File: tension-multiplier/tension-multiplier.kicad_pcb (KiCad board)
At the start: 2 copper layers, 18 x 13 mm, 4 parts, among them J1 Conn_01x03_Pin, J2 Conn_01x02_Pin, J3 Conn_01x02_Pin, U1 AD633ARZ

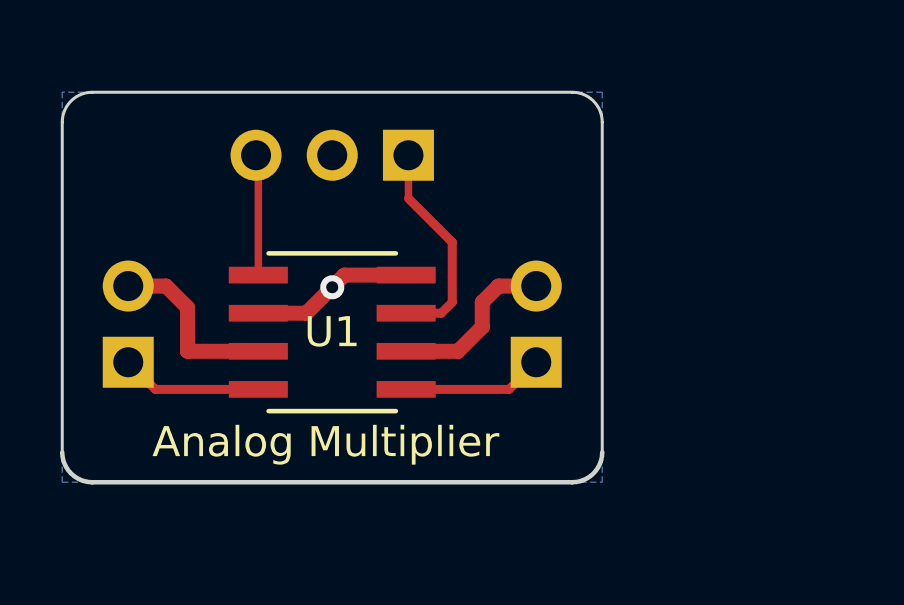
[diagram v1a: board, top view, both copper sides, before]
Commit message: Changes dimentions of the tension multiplier
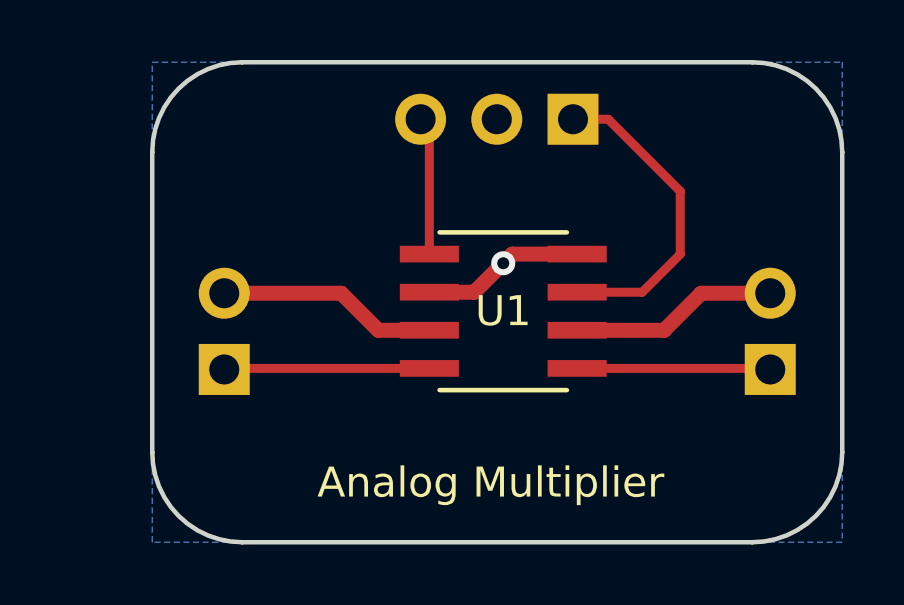
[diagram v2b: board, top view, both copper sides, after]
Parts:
- moved J2 7.80 mm to (158.6, 90.2)
- moved U1 5.74 mm to (149.7, 88.3)
- moved J1 5.61 mm to (152.0, 81.9)
- moved J3 3.21 mm to (140.4, 90.2)
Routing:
- net Net-(J1-Pin_1): track 7.19 -> 10.6 mm
- net Net-(J3-Pin_1): track 4.71 -> 6.85 mm
- net Net-(J2-Pin_1): track 4.71 -> 6.45 mm
- net VEE: track 6.09 -> 7.35 mm
- net VDD: track 5.72 -> 6.95 mm
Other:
- board size 18 x 13 mm -> 23 x 16 mm
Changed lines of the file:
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@@
   (net 7 "VEE")
   (footprint "footprints:R_8_ADI" (layer "F.Cu")
-    (at 144 89)
+    (at 149.7 88.3)
     (tags "AD633ARZ ")
     (property "Sheetfile" "tension-multiplier.kicad_sch")
@@
   )
   (footprint "Connector_PinHeader_2.54mm:PinHeader_1x03_P2.54mm_Vertical" (layer "B.Cu")
-    (at 146.54 83.1 90)
+    (at 152.025 81.9 90)
     (descr "Through hole straight pin header, 1x03, 2.54mm pitch, single row")
     (tags "Through hole pin header THT 1x03 2.54mm single row")
@@
   )
   (footprint "Connector_PinHeader_2.54mm:PinHeader_1x02_P2.54mm_Vertical" (layer "B.Cu")
-    (at 137.2 90)
+    (at 140.4 90.24)
     (descr "Through hole straight pin header, 1x02, 2.54mm pitch, single row")
     (tags "Through hole pin header THT 1x02 2.54mm single row")
@@
   )
   (footprint "Connector_PinHeader_2.54mm:PinHeader_1x02_P2.54mm_Vertical" (layer "B.Cu")
-    (at 150.8 90)
+    (at 158.6 90.24)
     (descr "Through hole straight pin header, 1x02, 2.54mm pitch, single row")
     (tags "Through hole pin header THT 1x02 2.54mm single row")
@@
     )
   )
-  (gr_line (start 135 93) (end 135 82)
-    (stroke (width 0.1) (type default)) (layer "Edge.Cuts"))
-  (gr_line (start 136 94) (end 152 94)
-    (stroke (width 0.15) (type default)) (layer "Edge.Cuts"))
-  (gr_line (start 136 81) (end 152 81)
-    (stroke (width 0.1) (type default)) (layer "Edge.Cuts"))
-  (gr_arc (start 135 82) (mid 135.292893 81.292893) (end 136 81)
-    (stroke (width 0.1) (type default)) (layer "Edge.Cuts"))
-  (gr_arc (start 152 81) (mid 152.707107 81.292893) (end 153 82)
-    (stroke (width 0.1) (type default)) (layer "Edge.Cuts"))
-  (gr_arc (start 136 94) (mid 135.292894 93.707107) (end 135 93)
-    (stroke (width 0.15) (type default)) (layer "Edge.Cuts"))
-  (gr_arc (start 153 93) (mid 152.707107 93.707106) (end 152 94)
-    (stroke (width 0.15) (type default)) (layer "Edge.Cuts"))
-  (gr_line (start 153 93) (end 153 82)
-    (stroke (width 0.1) (type default)) (layer "Edge.Cuts"))
-  (gr_text "Ux" (at 148 86) (layer "B.SilkS")
+  (gr_arc (start 161 93) (mid 160.12132 95.12132) (end 158 96)
+    (stroke (width 0.15) (type default)) (layer "Edge.Cuts"))
+  (gr_line (start 161 93) (end 161 83)
+    (stroke (width 0.15) (type default)) (layer "Edge.Cuts"))
+  (gr_line (start 141 96) (end 158 96)
+    (stroke (width 0.15) (type default)) (layer "Edge.Cuts"))
+  (gr_line (start 141 80) (end 158 80)
+    (stroke (width 0.15) (type default)) (layer "Edge.Cuts"))
+  (gr_arc (start 138 83) (mid 138.87868 80.87868) (end 141 80)
+    (stroke (width 0.15) (type default)) (layer "Edge.Cuts"))
+  (gr_arc (start 158 80) (mid 160.12132 80.87868) (end 161 83)
+    (stroke (width 0.15) (type default)) (layer "Edge.Cuts"))
+  (gr_arc (start 141 96) (mid 138.87868 95.12132) (end 138 93)
+    (stroke (width 0.15) (type default)) (layer "Edge.Cuts"))
+  (gr_line (start 138 93) (end 138 83)
+    (stroke (width 0.15) (type default)) (layer "Edge.Cuts"))
+  (gr_text "Ux" (at 153.66 84.8) (layer "B.SilkS")
     (effects (font (size 1 1) (thickness 0.2)) (justify left bottom mirror))
   )
-  (gr_text "Uz" (at 141 90.5) (layer "B.SilkS")
+  (gr_text "Uz" (at 144.1 90.74) (layer "B.SilkS")
     (effects (font (size 1 1) (thickness 0.2) bold) (justify left bottom mirror))
   )
-  (gr_text "V-" (at 141 88) (layer "B.SilkS")
+  (gr_text "V-" (at 144.2 88.24) (layer "B.SilkS")
     (effects (font (size 1 1) (thickness 0.2)) (justify left bottom mirror))
   )
-  (gr_text "Uw" (at 149 90.5) (layer "B.SilkS")
+  (gr_text "Uw" (at 156.6 90.7) (layer "B.SilkS")
     (effects (font (size 1 1) (thickness 0.2) bold) (justify left bottom mirror))
   )
-  (gr_text "V+" (at 149 88) (layer "B.SilkS")
+  (gr_text "V+" (at 156.8 88.24) (layer "B.SilkS")
     (effects (font (size 1 1) (thickness 0.2) bold) (justify left bottom mirror))
   )
-  (gr_text "Uy" (at 141.5 86) (layer "B.SilkS")
+  (gr_text "Uy" (at 147.16 84.8) (layer "B.SilkS")
     (effects (font (size 1 1) (thickness 0.2) bold) (justify left bottom mirror))
   )
-  (gr_text "GND" (at 145.5 86) (layer "B.SilkS")
+  (gr_text "GND" (at 151.16 84.8) (layer "B.SilkS")
     (effects (font (size 1 1) (thickness 0.2) bold) (justify left bottom mirror))
   )
-  (gr_text "Analog Multiplier" (at 138 93.25) (layer "F.SilkS")
+  (gr_text "Analog Multiplier" (at 143.5 94.6) (layer "F.SilkS")
     (effects (font (size 1 1) (thickness 0.2)) (justify left bottom))
   )
-  (segment (start 148 86) (end 148 88) (width 0.3) (layer "F.Cu") (net 1))
-  (segment (start 146.54 84.54) (end 146.54 83.1) (width 0.25) (layer "F.Cu") (net 1))
-  (segment (start 146.54 84.54) (end 148 86) (width 0.3) (layer "F.Cu") (net 1))
-  (segment (start 147.635 88.365) (end 146.4638 88.365) (width 0.3) (layer "F.Cu") (net 1))
-  (segment (start 148 88) (end 147.635 88.365) (width 0.3) (layer "F.Cu") (net 1))
-  (segment (start 141.5362 87.095) (end 141.5362 83.1762) (width 0.25) (layer "F.Cu") (net 2))
-  (segment (start 141.5362 83.1762) (end 141.46 83.1) (width 0.25) (layer "F.Cu") (net 2))
-  (segment (start 141.5362 83.0762) (end 141.46 83) (width 0.3) (layer "F.Cu") (net 2))
-  (segment (start 141.5362 87.095) (end 141.095 87.095) (width 0.5) (layer "F.Cu") (net 2))
-  (segment (start 150.8 90) (end 149.895 90.905) (width 0.3) (layer "F.Cu") (net 3))
-  (segment (start 149.895 90.905) (end 146.4638 90.905) (width 0.3) (layer "F.Cu") (net 3))
-  (segment (start 138.105 90.905) (end 141.5362 90.905) (width 0.3) (layer "F.Cu") (net 4))
-  (segment (start 137.2 90) (end 138.105 90.905) (width 0.3) (layer "F.Cu") (net 4))
-  (segment (start 149 88.825) (end 148.19 89.635) (width 0.5) (layer "F.Cu") (net 5))
-  (segment (start 148.19 89.635) (end 146.4638 89.635) (width 0.5) (layer "F.Cu") (net 5))
-  (segment (start 149 88) (end 149 88.825) (width 0.5) (layer "F.Cu") (net 5))
-  (segment (start 150.8 87.46) (end 149.54 87.46) (width 0.5) (layer "F.Cu") (net 5))
-  (segment (start 149.54 87.46) (end 149 88) (width 0.5) (layer "F.Cu") (net 5))
-  (segment (start 143.135 88.365) (end 144.405 87.095) (width 0.5) (layer "F.Cu") (net 6))
-  (segment (start 141.5362 88.365) (end 143.135 88.365) (width 0.5) (layer "F.Cu") (net 6))
-  (segment (start 144.405 87.095) (end 146.4638 87.095) (width 0.5) (layer "F.Cu") (net 6))
-  (via (at 144 87.5) (size 0.8) (drill 0.4) (layers "F.Cu" "B.Cu") (net 6))
-  (segment (start 141.5362 89.635) (end 139.175 89.635) (width 0.5) (layer "F.Cu") (net 7))
-  (segment (start 138.46 87.46) (end 137.2 87.46) (width 0.5) (layer "F.Cu") (net 7))
-  (segment (start 139.175 89.635) (end 139.175 88.175) (width 0.5) (layer "F.Cu") (net 7))
-  (segment (start 139.175 88.175) (end 138.46 87.46) (width 0.5) (layer "F.Cu") (net 7))
+  (segment (start 152.1638 87.665) (end 154.335 87.665) (width 0.3) (layer "F.Cu") (net 1))
+  (segment (start 155.6 84.3) (end 153.2 81.9) (width 0.3) (layer "F.Cu") (net 1))
+  (segment (start 153.2 81.9) (end 152.025 81.9) (width 0.3) (layer "F.Cu") (net 1))
+  (segment (start 155.6 86.4) (end 155.6 84.3) (width 0.3) (layer "F.Cu") (net 1))
+  (segment (start 154.335 87.665) (end 155.6 86.4) (width 0.3) (layer "F.Cu") (net 1))
+  (segment (start 147.2362 82.1912) (end 146.945 81.9) (width 0.3) (layer "F.Cu") (net 2))
+  (segment (start 147.1962 81.9762) (end 147.12 81.9) (width 0.3) (layer "F.Cu") (net 2))
+  (segment (start 147.2362 86.395) (end 147.2362 82.1912) (width 0.3) (layer "F.Cu") (net 2))
+  (segment (start 152.1638 90.205) (end 158.565 90.205) (width 0.3) (layer "F.Cu") (net 3))
+  (segment (start 158.565 90.205) (end 158.6 90.24) (width 0.3) (layer "F.Cu") (net 3))
+  (segment (start 147.2362 90.205) (end 140.435 90.205) (width 0.3) (layer "F.Cu") (net 4))
+  (segment (start 140.435 90.205) (end 140.4 90.24) (width 0.3) (layer "F.Cu") (net 4))
+  (segment (start 152.1638 88.935) (end 155.065 88.935) (width 0.5) (layer "F.Cu") (net 5))
+  (segment (start 156.3 87.7) (end 158.6 87.7) (width 0.5) (layer "F.Cu") (net 5))
+  (segment (start 155.065 88.935) (end 156.3 87.7) (width 0.5) (layer "F.Cu") (net 5))
+  (segment (start 148.735 87.665) (end 149.7 86.7) (width 0.5) (layer "F.Cu") (net 6))
+  (segment (start 147.2362 87.665) (end 148.735 87.665) (width 0.5) (layer "F.Cu") (net 6))
+  (segment (start 152.1638 86.395) (end 150.005 86.395) (width 0.5) (layer "F.Cu") (net 6))
+  (segment (start 150.005 86.395) (end 149.7 86.7) (width 0.5) (layer "F.Cu") (net 6))
+  (via (at 149.7 86.7) (size 0.8) (drill 0.4) (layers "F.Cu" "B.Cu") (net 6))
+  (segment (start 149.7 82.115) (end 149.485 81.9) (width 0.5) (layer "B.Cu") (net 6))
+  (segment (start 144.3 87.7) (end 145.535 88.935) (width 0.5) (layer "F.Cu") (net 7))
+  (segment (start 140.4 87.7) (end 144.3 87.7) (width 0.5) (layer "F.Cu") (net 7))
+  (segment (start 145.535 88.935) (end 147.2362 88.935) (width 0.5) (layer "F.Cu") (net 7))
   (zone (net 6) (net_name "GND") (layer "B.Cu") (hatch edge 0.5)
     (connect_pads (clearance 0.3))
@@
     (polygon
       (pts
-        (xy 135 81)
-        (xy 135 94)
-        (xy 153 94)
-        (xy 153 81)
+        (xy 138 80)
+        (xy 161 80)
+        (xy 161 96)
+        (xy 138 96)
       )
     )

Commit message: Refactors modules pcblayout to cosmetic purposes
Also, refactors Amplifiers moduleboard to include a VEE plane
(powerplane).
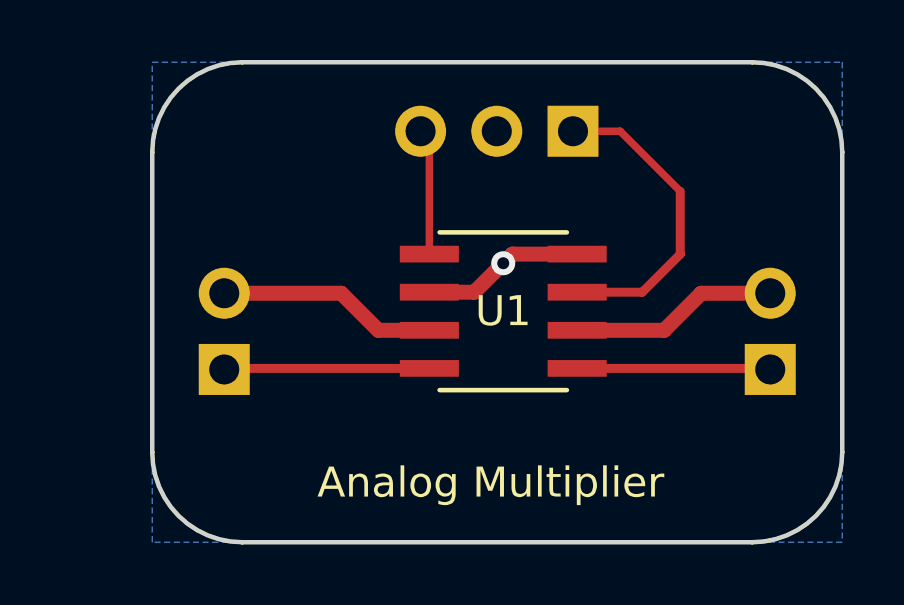
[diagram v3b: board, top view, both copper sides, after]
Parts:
- moved J1 0.40 mm to (152.0, 82.3)
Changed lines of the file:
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@@
   (setup
     (stackup
-      (layer "F.SilkS" (type "Top Silk Screen"))
+      (layer "F.SilkS" (type "Top Silk Screen") (color "White"))
       (layer "F.Paste" (type "Top Solder Paste"))
-      (layer "F.Mask" (type "Top Solder Mask") (thickness 0.01))
+      (layer "F.Mask" (type "Top Solder Mask") (color "Black") (thickness 0.01))
       (layer "F.Cu" (type "copper") (thickness 0.035))
       (layer "dielectric 1" (type "core") (thickness 1.51) (material "FR4") (epsilon_r 4.5) (loss_tangent 0.02))
       (layer "B.Cu" (type "copper") (thickness 0.035))
-      (layer "B.Mask" (type "Bottom Solder Mask") (thickness 0.01))
+      (layer "B.Mask" (type "Bottom Solder Mask") (color "Black") (thickness 0.01))
       (layer "B.Paste" (type "Bottom Solder Paste"))
-      (layer "B.SilkS" (type "Bottom Silk Screen"))
+      (layer "B.SilkS" (type "Bottom Silk Screen") (color "White"))
       (copper_finish "None")
       (dielectric_constraints no)
@@
   )
   (footprint "Connector_PinHeader_2.54mm:PinHeader_1x03_P2.54mm_Vertical" (layer "B.Cu")
-    (at 152.025 81.9 90)
+    (at 152.025 82.3 90)
     (descr "Through hole straight pin header, 1x03, 2.54mm pitch, single row")
     (tags "Through hole pin header THT 1x03 2.54mm single row")
@@
   (gr_line (start 138 93) (end 138 83)
     (stroke (width 0.15) (type default)) (layer "Edge.Cuts"))
-  (gr_text "Ux" (at 153.66 84.8) (layer "B.SilkS")
+  (gr_text "Ux" (at 153.66 85.2) (layer "B.SilkS")
     (effects (font (size 1 1) (thickness 0.2)) (justify left bottom mirror))
   )
@@
     (effects (font (size 1 1) (thickness 0.2) bold) (justify left bottom mirror))
   )
-  (gr_text "Uy" (at 147.16 84.8) (layer "B.SilkS")
+  (gr_text "Uy" (at 147.16 85.2) (layer "B.SilkS")
     (effects (font (size 1 1) (thickness 0.2) bold) (justify left bottom mirror))
   )
-  (gr_text "GND" (at 151.16 84.8) (layer "B.SilkS")
+  (gr_text "GND" (at 151.16 85.2) (layer "B.SilkS")
     (effects (font (size 1 1) (thickness 0.2) bold) (justify left bottom mirror))
   )
@@
     (effects (font (size 1 1) (thickness 0.2)) (justify left bottom))
   )
+  (segment (start 153.6 82.3) (end 152.025 82.3) (width 0.25) (layer "F.Cu") (net 1))
   (segment (start 152.1638 87.665) (end 154.335 87.665) (width 0.3) (layer "F.Cu") (net 1))
-  (segment (start 155.6 84.3) (end 153.2 81.9) (width 0.3) (layer "F.Cu") (net 1))
-  (segment (start 153.2 81.9) (end 152.025 81.9) (width 0.3) (layer "F.Cu") (net 1))
+  (segment (start 155.6 84.3) (end 153.6 82.3) (width 0.25) (layer "F.Cu") (net 1))
   (segment (start 155.6 86.4) (end 155.6 84.3) (width 0.3) (layer "F.Cu") (net 1))
   (segment (start 154.335 87.665) (end 155.6 86.4) (width 0.3) (layer "F.Cu") (net 1))
   (segment (start 147.2362 82.1912) (end 146.945 81.9) (width 0.3) (layer "F.Cu") (net 2))
   (segment (start 147.1962 81.9762) (end 147.12 81.9) (width 0.3) (layer "F.Cu") (net 2))
-  (segment (start 147.2362 86.395) (end 147.2362 82.1912) (width 0.3) (layer "F.Cu") (net 2))
+  (segment (start 147.2362 82.5912) (end 146.945 82.3) (width 0.25) (layer "F.Cu") (net 2))
+  (segment (start 147.2362 86.395) (end 147.2362 82.5912) (width 0.25) (layer "F.Cu") (net 2))
   (segment (start 152.1638 90.205) (end 158.565 90.205) (width 0.3) (layer "F.Cu") (net 3))
   (segment (start 158.565 90.205) (end 158.6 90.24) (width 0.3) (layer "F.Cu") (net 3))

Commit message: Add JLCPCB serial number to the module pcbs
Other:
- board text added: "JLCJLCJLCJLC"
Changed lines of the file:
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@@
     (effects (font (size 1 1) (thickness 0.2)) (justify left bottom mirror))
+  )
+  (gr_text "JLCJLCJLCJLC" (at 154 94.6) (layer "B.SilkS")
+    (effects (font (size 0.8 0.8) (thickness 0.15)) (justify left bottom mirror))
   )
   (gr_text "Uw" (at 156.6 90.7) (layer "B.SilkS")
